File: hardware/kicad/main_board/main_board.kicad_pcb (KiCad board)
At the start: 2 copper layers, 76.2 x 76.2 mm, 1 part, among them J1 Conn_01x04_MountingPin

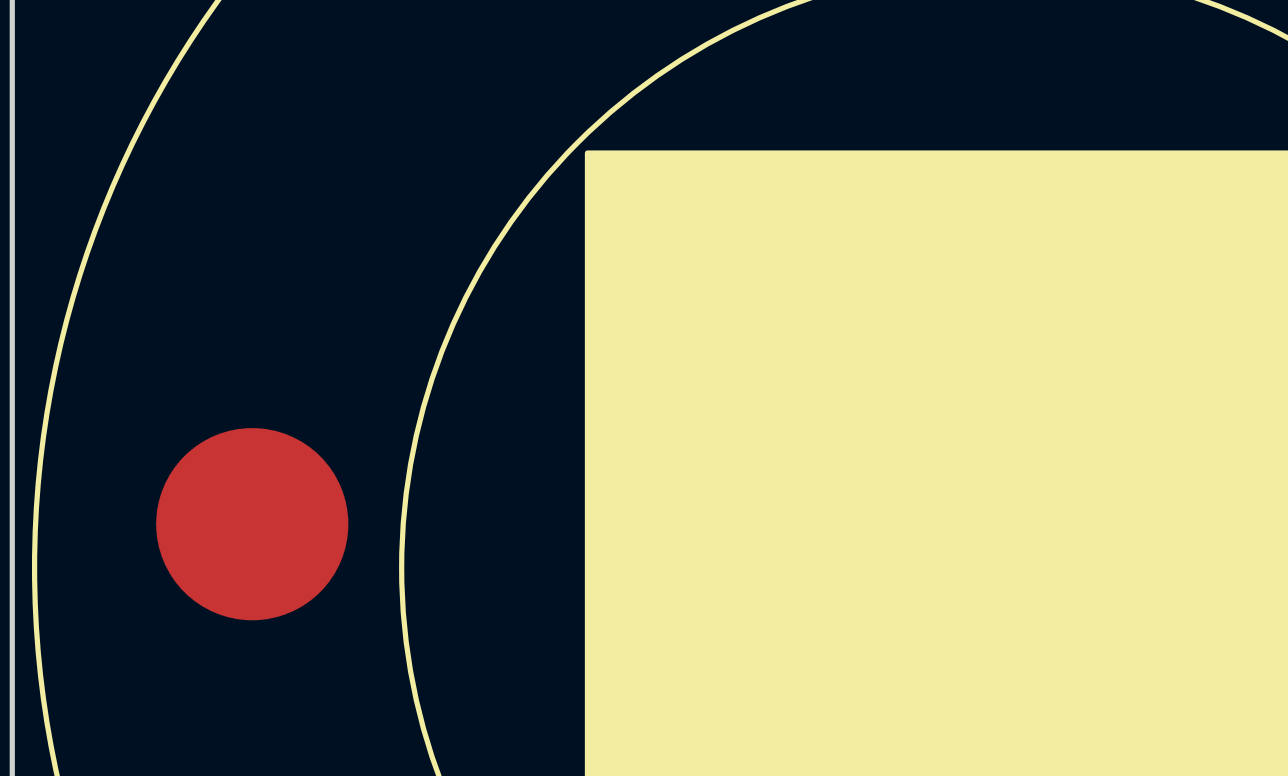
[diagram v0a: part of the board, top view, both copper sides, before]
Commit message: Adding initial PCB and touch ring files
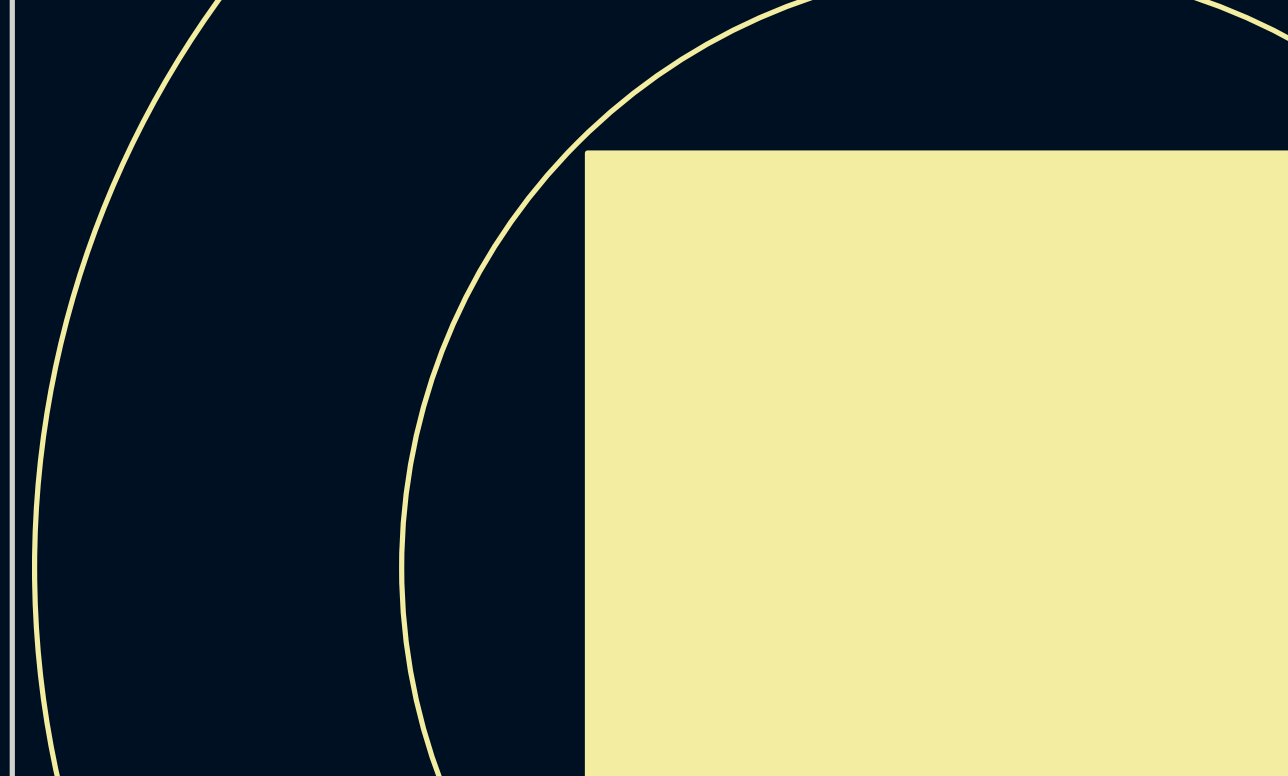
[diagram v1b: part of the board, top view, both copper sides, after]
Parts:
- J1: footprint Connector_PinHeader_1.00mm:PinHeader_1x04_P1.00mm_Vertical -> Connector_PinSocket_1.00mm:PinSocket_1x04_P1.00mm_Vertical
- moved J1 2.54 mm to (139.7, 73.7)
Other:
- board text added: "https://sdumetz.github.io/2016/08/15/capacitive-wheel.html"
